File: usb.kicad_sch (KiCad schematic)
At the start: 5 parts, among them J14 USB_C_Receptacle_USB2.0_16P

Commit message: 24V Regulator, Pyro Igniter Circuit
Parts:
- renumbered J14 to J12
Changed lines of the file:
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@@
 		(dnp no)
 		(fields_autoplaced yes)
-		(property "Reference" "#PWR097"
+		(property "Reference" "#PWR093"
 			(at 130.81 121.92 0)
 			(hide yes)
@@
 			(project "mixed_signal_sensor_board"
 				(path "/5c142d60-6b5a-463f-88b9-a177eae7f51b/0f186850-c4c3-487e-83d6-f05a4c56befe"
-					(reference "#PWR097")
+					(reference "#PWR093")
 					(unit 1)
 				)
@@
 		(dnp no)
 		(fields_autoplaced yes)
-		(property "Reference" "J14"
+		(property "Reference" "J12"
 			(at 138.43 69.85 0)
 			(show_name no)
@@
 			(project "mixed_signal_sensor_board"
 				(path "/5c142d60-6b5a-463f-88b9-a177eae7f51b/0f186850-c4c3-487e-83d6-f05a4c56befe"
-					(reference "J14")
+					(reference "J12")
 					(unit 1)
 				)
@@
 		(dnp no)
 		(fields_autoplaced yes)
-		(property "Reference" "#PWR098"
+		(property "Reference" "#PWR094"
 			(at 161.29 123.19 0)
 			(hide yes)
@@
 			(project "mixed_signal_sensor_board"
 				(path "/5c142d60-6b5a-463f-88b9-a177eae7f51b/0f186850-c4c3-487e-83d6-f05a4c56befe"
-					(reference "#PWR098")
+					(reference "#PWR094")
 					(unit 1)
 				)

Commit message: Delvin protection, USB ESD protection, 02x06 pin socket
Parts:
- added U8: USBLC6-2P6, Package_TO_SOT_SMD:SOT-666, symbol Power_Protection:USBLC6-2P6
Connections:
- net GND: now also U8.2 (GND)
- net USB_N: now also U8.6 (I/O1); no longer R48.2
- net USB_P: now also U8.4 (I/O2); no longer R49.2
- new net: R48.2, U8.1 (I/O1)
- new net: R49.2, U8.3 (I/O2)
- no-connect marks 3 -> 4

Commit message: replaced signal blocks, shortening board, adding precise positioning
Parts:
- renumbered J12 to J13, R46 to R47, R47 to R48, R48 to R49, R49 to R50
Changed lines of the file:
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@@
 		(dnp no)
 		(fields_autoplaced yes)
-		(property "Reference" "#PWR099"
+		(property "Reference" "#PWR0104"
 			(at 130.81 121.92 0)
 			(hide yes)
@@
 			(project "mixed_signal_sensor_board"
 				(path "/5c142d60-6b5a-463f-88b9-a177eae7f51b/0f186850-c4c3-487e-83d6-f05a4c56befe"
-					(reference "#PWR099")
+					(reference "#PWR0104")
 					(unit 1)
 				)
@@
 		(dnp no)
 		(fields_autoplaced yes)
-		(property "Reference" "J12"
+		(property "Reference" "J13"
 			(at 138.43 69.85 0)
 			(show_name no)
@@
 			(project "mixed_signal_sensor_board"
 				(path "/5c142d60-6b5a-463f-88b9-a177eae7f51b/0f186850-c4c3-487e-83d6-f05a4c56befe"
-					(reference "J12")
+					(reference "J13")
 					(unit 1)
 				)
@@
 		(in_pos_files yes)
 		(dnp no)
-		(property "Reference" "R48"
+		(property "Reference" "R49"
 			(at 170.18 85.852 90)
 			(show_name no)
@@
 			(project "mixed_signal_sensor_board"
 				(path "/5c142d60-6b5a-463f-88b9-a177eae7f51b/0f186850-c4c3-487e-83d6-f05a4c56befe"
-					(reference "R48")
+					(reference "R49")
 					(unit 1)
 				)
@@
 		(in_pos_files yes)
 		(dnp no)
-		(property "Reference" "R49"
+		(property "Reference" "R50"
 			(at 170.18 93.218 90)
 			(show_name no)
@@
 			(project "mixed_signal_sensor_board"
 				(path "/5c142d60-6b5a-463f-88b9-a177eae7f51b/0f186850-c4c3-487e-83d6-f05a4c56befe"
-					(reference "R49")
+					(reference "R50")
 					(unit 1)
 				)
@@
 		(in_pos_files yes)
 		(dnp no)
-		(property "Reference" "R46"
+		(property "Reference" "R47"
 			(at 152.908 113.03 90)
 			(show_name no)
@@
 			(project "mixed_signal_sensor_board"
 				(path "/5c142d60-6b5a-463f-88b9-a177eae7f51b/0f186850-c4c3-487e-83d6-f05a4c56befe"
-					(reference "R46")
+					(reference "R47")
 					(unit 1)
 				)
@@
 		(dnp no)
 		(fields_autoplaced yes)
-		(property "Reference" "#PWR0100"
+		(property "Reference" "#PWR0105"
 			(at 161.29 123.19 0)
 			(hide yes)
@@
 			(project "mixed_signal_sensor_board"
 				(path "/5c142d60-6b5a-463f-88b9-a177eae7f51b/0f186850-c4c3-487e-83d6-f05a4c56befe"
-					(reference "#PWR0100")
+					(reference "#PWR0105")
 					(unit 1)
 				)
@@
 		(dnp no)
 		(fields_autoplaced yes)
-		(property "Reference" "#PWR0101"
+		(property "Reference" "#PWR0106"
 			(at 184.15 106.68 0)
 			(hide yes)
@@
 			(project "mixed_signal_sensor_board"
 				(path "/5c142d60-6b5a-463f-88b9-a177eae7f51b/0f186850-c4c3-487e-83d6-f05a4c56befe"
-					(reference "#PWR0101")
+					(reference "#PWR0106")
 					(unit 1)
 				)
@@
 		(in_pos_files yes)
 		(dnp no)
-		(property "Reference" "R47"
+		(property "Reference" "R48"
 			(at 160.528 113.03 90)
 			(show_name no)
@@
 			(project "mixed_signal_sensor_board"
 				(path "/5c142d60-6b5a-463f-88b9-a177eae7f51b/0f186850-c4c3-487e-83d6-f05a4c56befe"
-					(reference "R47")
+					(reference "R48")
 					(unit 1)
 				)

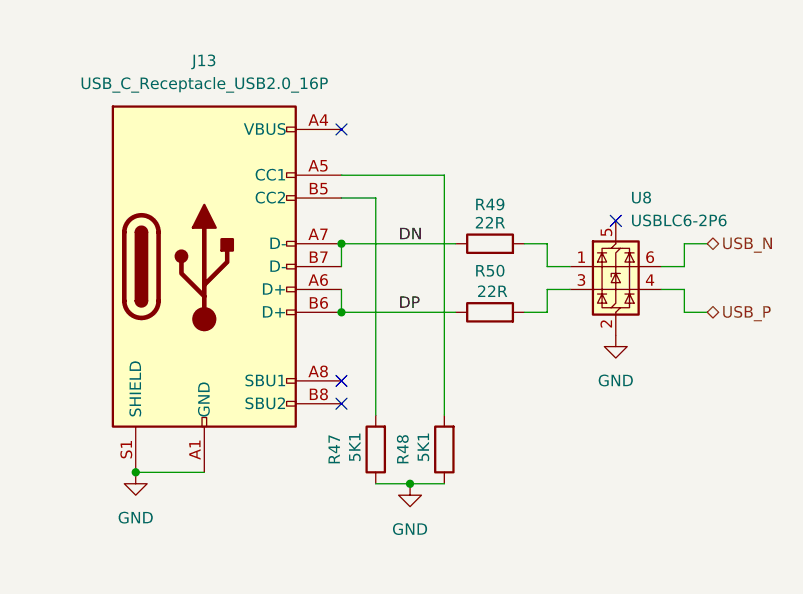
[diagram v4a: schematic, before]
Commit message: PYRO done, schematic structure/convention update, pyro and reverse polarity components selected
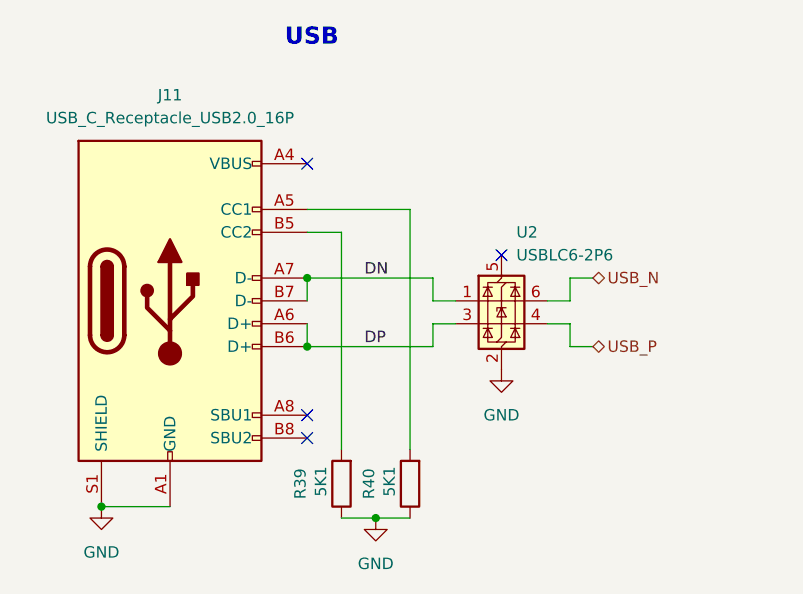
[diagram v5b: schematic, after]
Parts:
- removed R49, R50: 22R, Resistor_SMD:R_0402_1005Metric, symbol Device:R
- renumbered J13 to J11, R47 to R39, R48 to R40, U8 to U2
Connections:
- net DN: now also U2.1 (I/O1)
- net DP: now also U2.3 (I/O2)
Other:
- note added: "USB"
- moved on the sheet: J11, R39, R40, U2
